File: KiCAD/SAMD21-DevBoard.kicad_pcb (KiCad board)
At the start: 2 copper layers, 44 x 60 mm, 35 parts, among them J1 .1" Headers, J2 .1" Headers, J3 Cortex_Debug, J4 USB-Micro, Q1 3.7A, 30V, SW1 FSMCTTR, U1 SAMD21G18A-AU, U2 LM1117, U3 AP2112K-3.3, Y1 32.768KHz

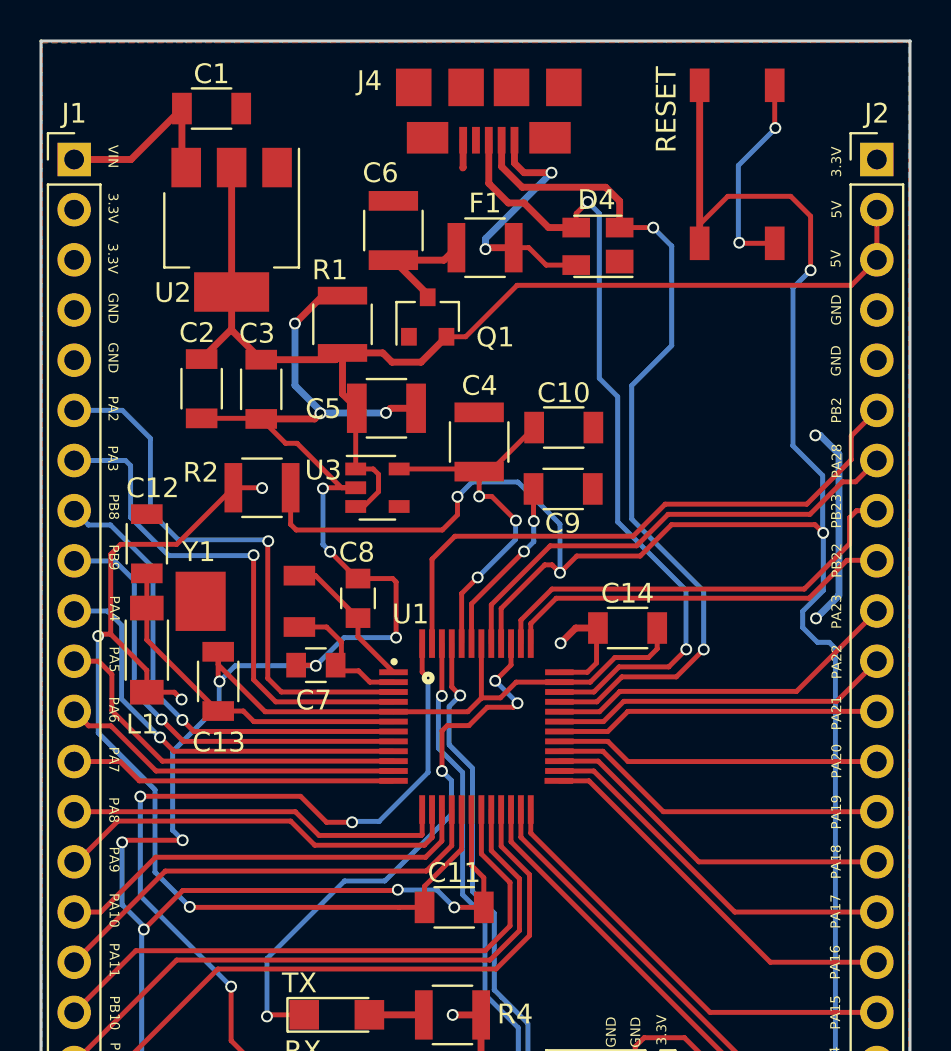
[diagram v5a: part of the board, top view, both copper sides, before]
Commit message: Attempting to increase top flood plane connectivity
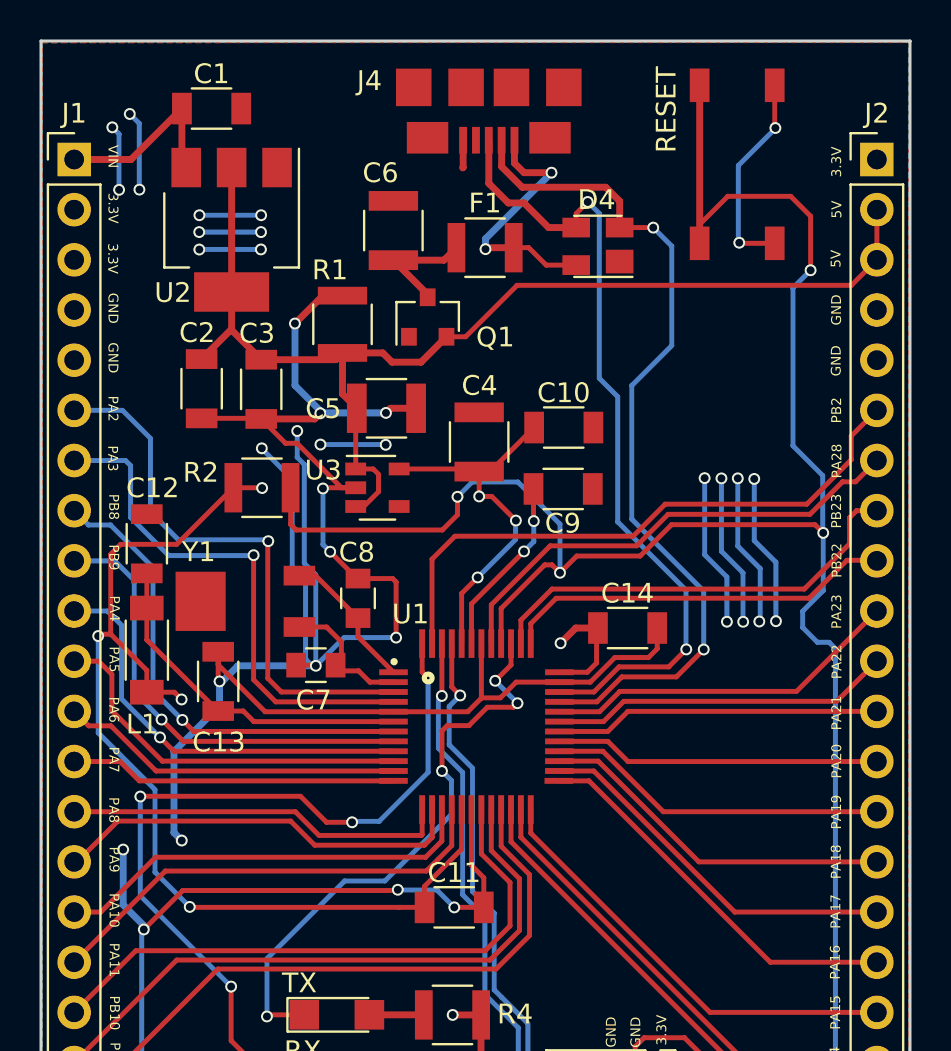
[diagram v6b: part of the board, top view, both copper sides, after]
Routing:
- net (no net): track 10.4 -> 50.9 mm, vias 2 -> 20
- net GND: track 183.9 -> 204.9 mm, vias 16 -> 18

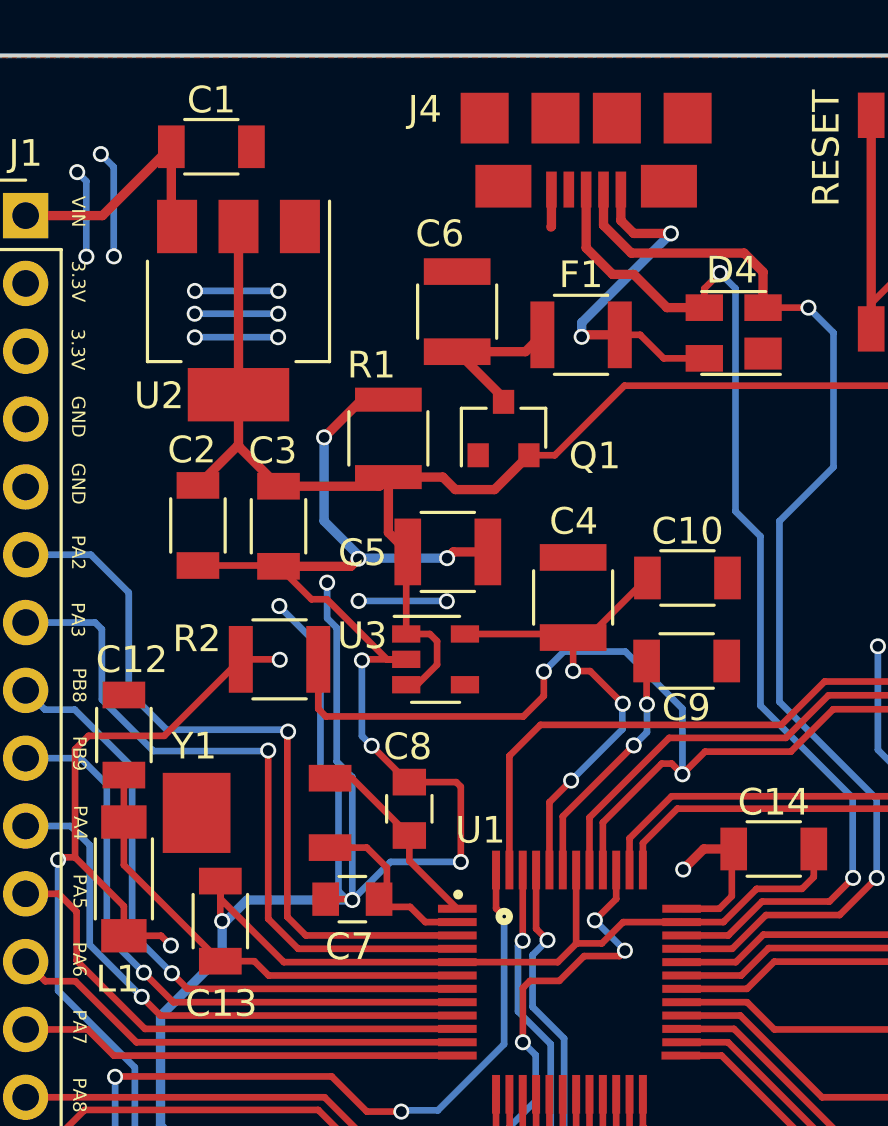
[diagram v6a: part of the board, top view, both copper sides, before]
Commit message: Revised crystal symbol and updated layout slightly
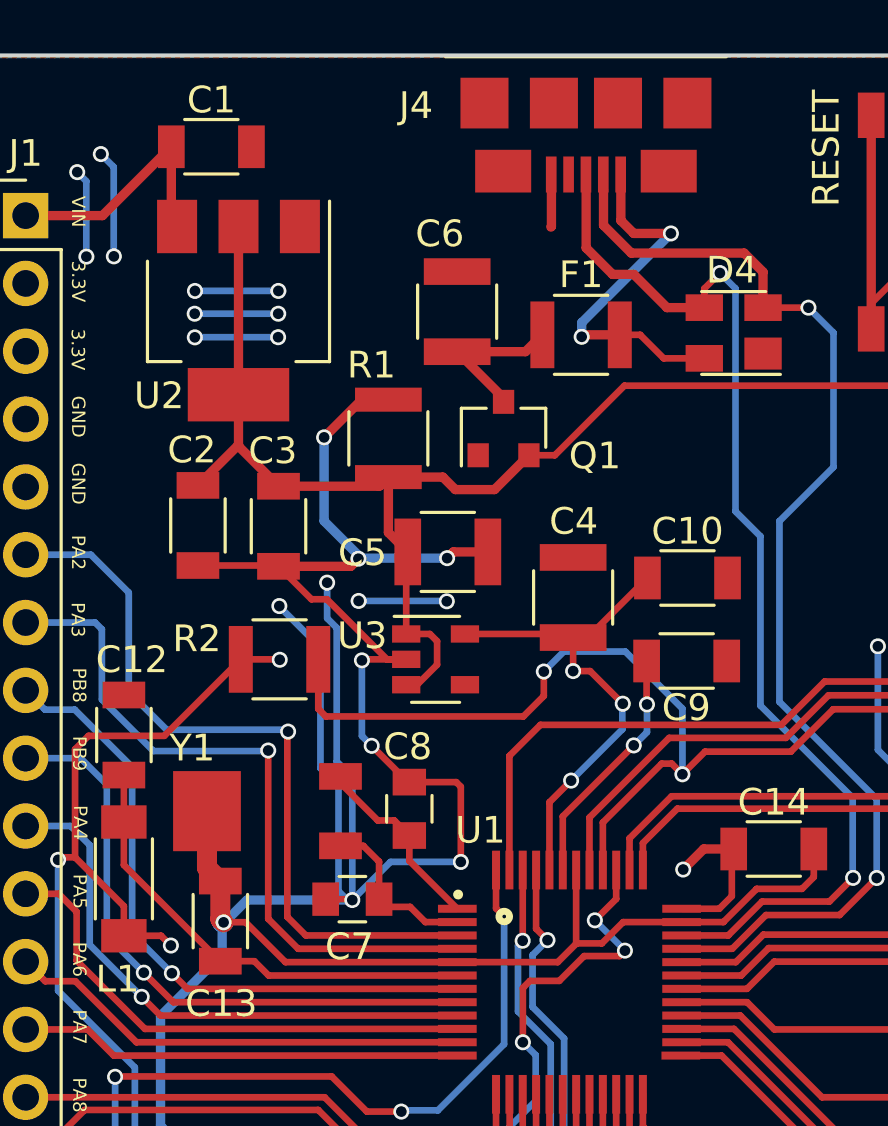
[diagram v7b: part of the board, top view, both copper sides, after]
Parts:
- Y1: value 32.768KHz -> 32.768kHz
- moved J4 0.56 mm to (149.7, 51.8)
- moved Y1 0.39 mm to (137.6, 78.3)
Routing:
- net GND: track 204.9 -> 207.8 mm
- net VBUS: track 13.5 -> 14.6 mm
- net USB_D+: track 41.1 -> 42.2 mm
- net USB_D-: track 43.6 -> 44.7 mm
